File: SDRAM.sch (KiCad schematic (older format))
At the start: 28 parts

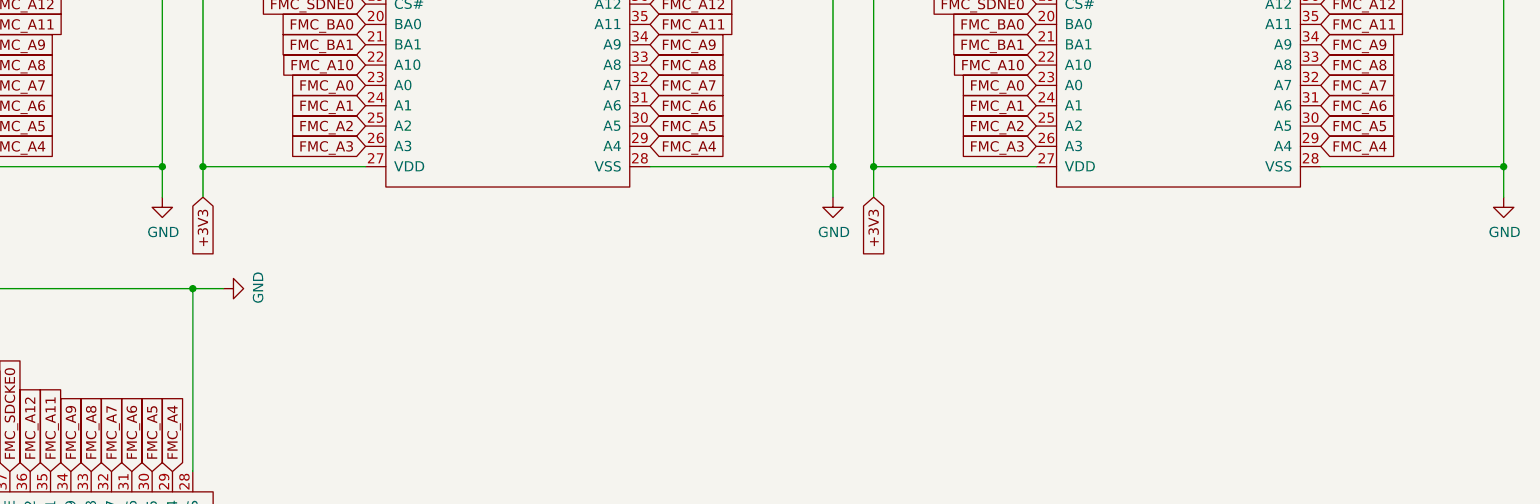
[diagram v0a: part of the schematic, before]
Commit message: First proposed pin layout of SODIMM connector
Will need to add GPIO / ADC pins as needed, but let's wait to see if we don't
need to use more pins.

Double-checked and fixed CODEC and MCU's power supply.
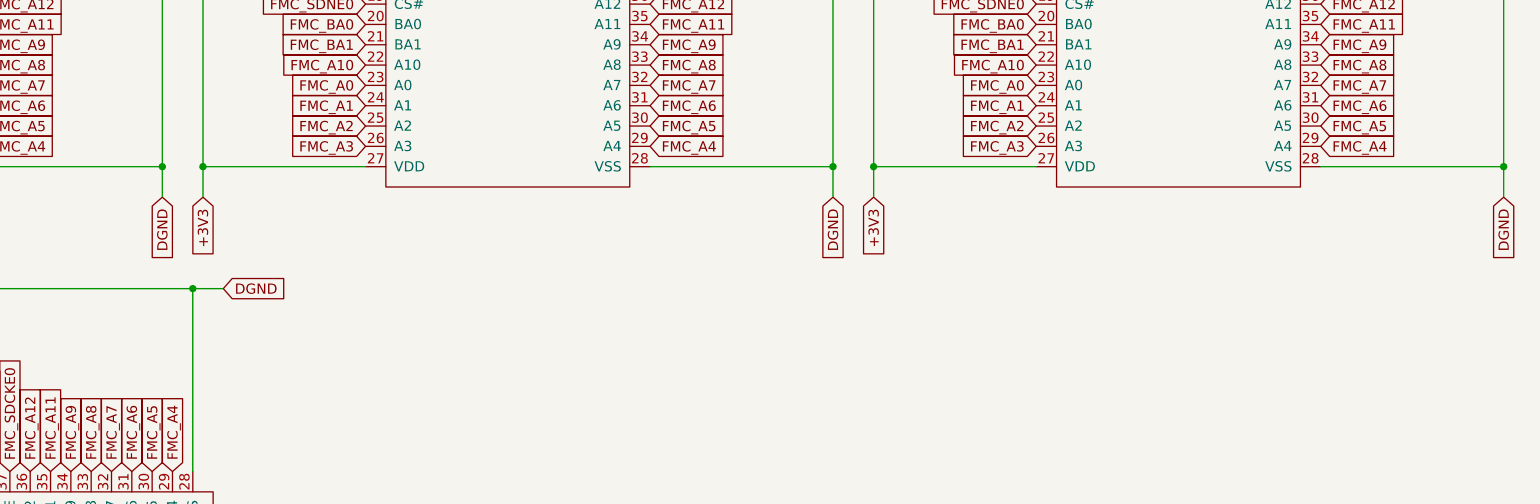
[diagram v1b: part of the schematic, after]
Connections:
- net GND renamed DGND
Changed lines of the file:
@@
 $Descr A4 11693 8268
 encoding utf-8
-Sheet 7 12
+Sheet 7 13
 Title ""
 Date ""
@@
 	650  3850 650  4000
 Connection ~ 650  3850
-$Comp
-L power:GND #PWR?
-U 1 1 5CFE16C9
-P 3750 4000
-F 0 "#PWR?" H 3750 3750 50  0001 C CNN
-F 1 "GND" H 3755 3827 50  0000 C CNN
-F 2 "" H 3750 4000 50  0001 C CNN
-F 3 "" H 3750 4000 50  0001 C CNN
-	1    3750 4000
-	1    0    0    -1
-$EndComp
 Wire Wire Line
 	3750 3850 3750 4000
@@
 	3950 3850 3950 4000
 Connection ~ 3950 3850
-$Comp
-L power:GND #PWR?
-U 1 1 5CFE3057
-P 7050 4000
-F 0 "#PWR?" H 7050 3750 50  0001 C CNN
-F 1 "GND" H 7055 3827 50  0000 C CNN
-F 2 "" H 7050 4000 50  0001 C CNN
-F 3 "" H 7050 4000 50  0001 C CNN
-	1    7050 4000
-	1    0    0    -1
-$EndComp
 Wire Wire Line
 	7050 3850 7050 4000
@@
 	7250 3850 7250 4000
 Connection ~ 7250 3850
-$Comp
-L power:GND #PWR?
-U 1 1 5CFE5464
-P 10350 4000
-F 0 "#PWR?" H 10350 3750 50  0001 C CNN
-F 1 "GND" H 10355 3827 50  0000 C CNN
-F 2 "" H 10350 4000 50  0001 C CNN
-F 3 "" H 10350 4000 50  0001 C CNN
-	1    10350 4000
-	1    0    0    -1
-$EndComp
 Wire Wire Line
 	10350 3850 10350 4000
@@
 	3900 7550 4050 7550
 Connection ~ 3900 7550
-$Comp
-L power:GND #PWR?
-U 1 1 5CFED4CF
-P 4050 4450
-F 0 "#PWR?" H 4050 4200 50  0001 C CNN
-F 1 "GND" H 4055 4277 50  0000 C CNN
-F 2 "" H 4050 4450 50  0001 C CNN
-F 3 "" H 4050 4450 50  0001 C CNN
-	1    4050 4450
-	0    -1   -1   0
-$EndComp
 Wire Wire Line
 	3900 4450 4050 4450
@@
 Text Notes 800  550  0    50   ~ 0
 Decoupling capacitors, place close to VDD pins on SDRAM
+Text GLabel 3750 4000 3    50   Input ~ 0
+DGND
+Text GLabel 7050 4000 3    50   Input ~ 0
+DGND
+Text GLabel 10350 4000 3    50   Input ~ 0
+DGND
+Text GLabel 4050 4450 2    50   Input ~ 0
+DGND
 $EndSCHEMATC
